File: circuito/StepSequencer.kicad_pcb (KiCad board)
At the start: 2 copper layers, 126.5 x 117.1 mm, 89 parts, among them P1 BEAGLEBONE_BLACK, P2 CONN_01X01, P3 CONN_01X01, P4 CONN_01X01, P5 CONN_01X01, SW0 SW_PUSH, SW1 SW_PUSH, SW10 SW_PUSH, SW11 SW_PUSH, SW12 SW_PUSH, SW13 SW_PUSH, SW14 SW_PUSH, SW15 SW_PUSH, SW2 SW_PUSH, SW3 SW_PUSH, SW4 SW_PUSH, SW5 SW_PUSH, SW6 SW_PUSH, SW7 SW_PUSH, SW8 SW_PUSH, SW9 SW_PUSH

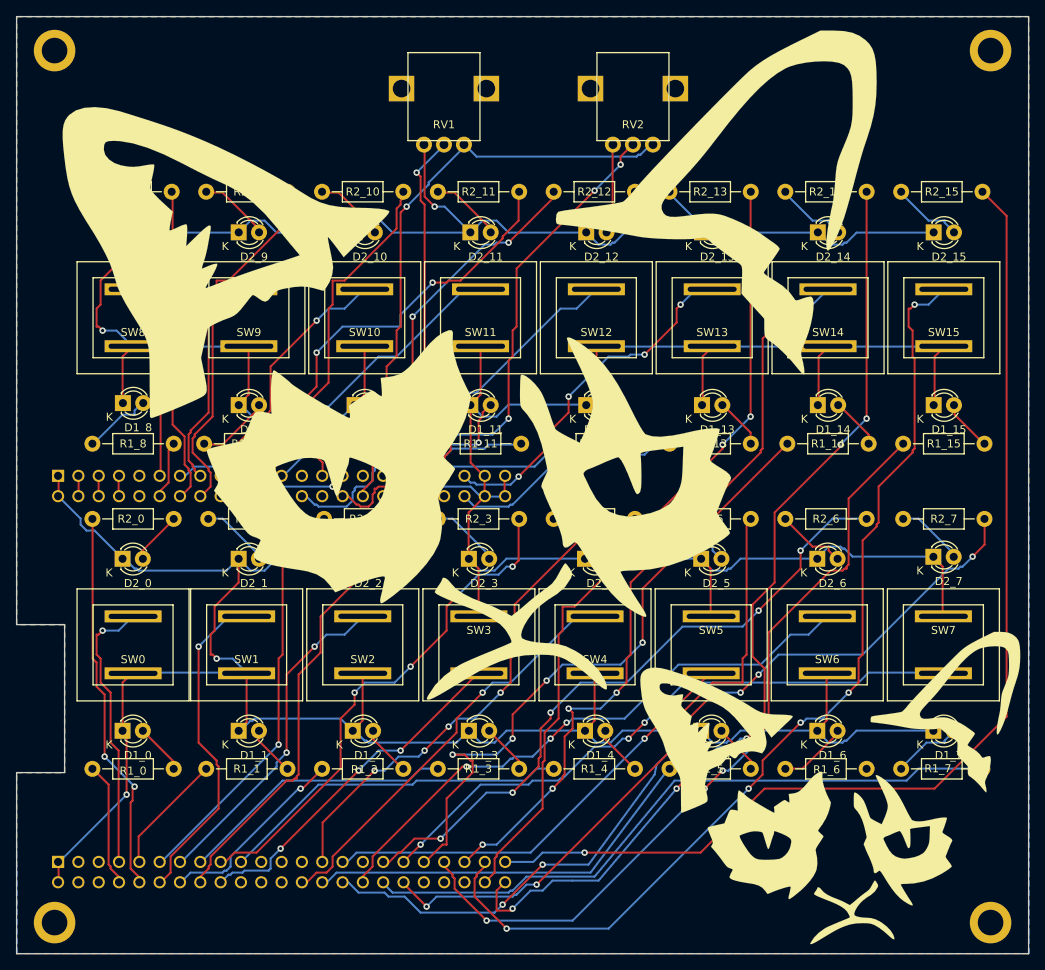
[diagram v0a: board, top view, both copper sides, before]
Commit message: arreglados huecos corte botones y botones footprints
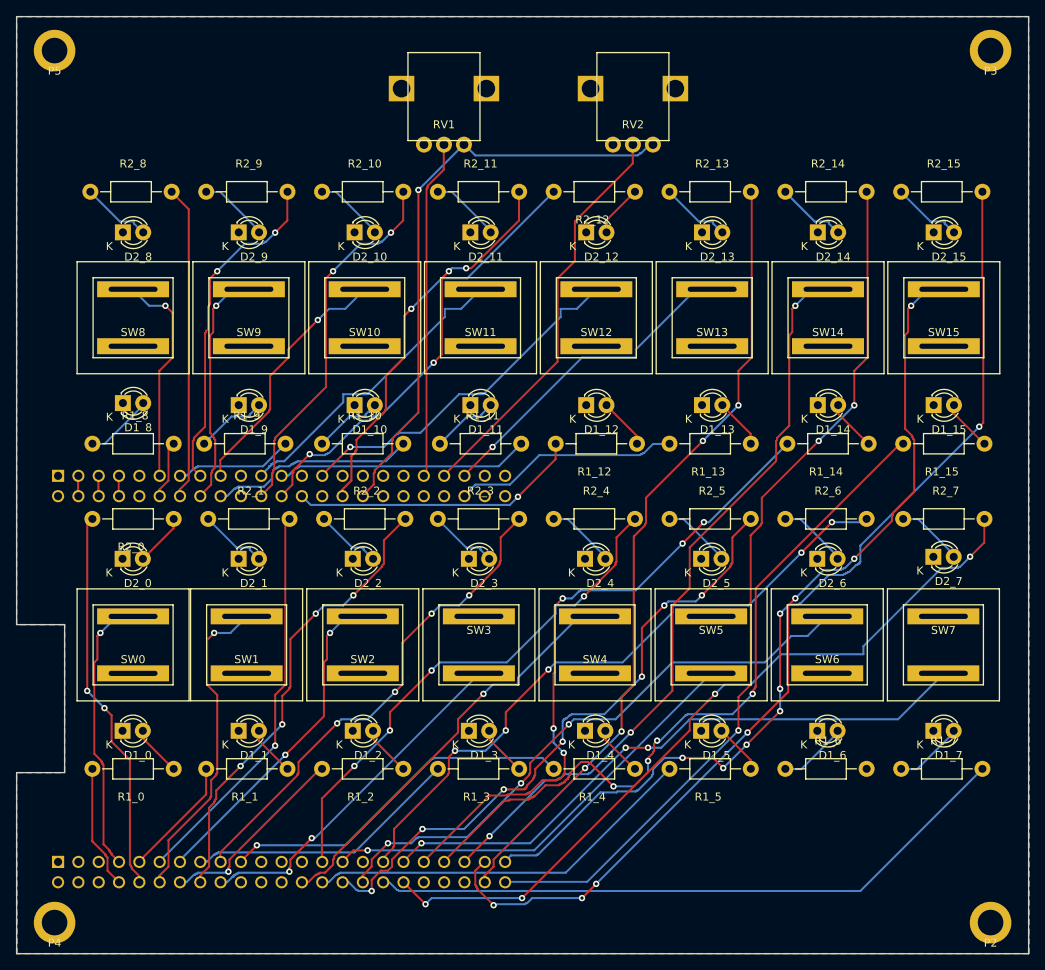
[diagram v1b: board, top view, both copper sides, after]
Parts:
- removed G***: LOGO, StepSequencer:GATO3
- removed G***: LOGO, StepSequencer:GATO2
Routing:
- net GNDD: track 700.0 -> 0.00 mm, vias 4 -> 0
- net /led2_15: track 137.1 -> 121.4 mm, vias 1 -> 7
- net /led2_11: track 63.6 -> 54.3 mm, vias 2 -> 4
- net /led2_14: track 120.5 -> 111.2 mm, vias 6 -> 3
- net /led2_5: track 87.9 -> 80.1 mm, vias 3 -> 7
- net /led1_15: track 98.5 -> 91.2 mm
- net /btn15: track 123.9 -> 116.8 mm, vias 5 -> 7
- net /btn12: track 49.2 -> 44.6 mm, vias 3 -> 1
- net /led2_12: track 55.3 -> 50.9 mm, vias 2 -> 1
- net /btn13: track 45.0 -> 41.3 mm, vias 4 -> 1
- net /pot1: track 54.3 -> 51.3 mm, vias 4 -> 0
- net /led2_3: track 64.6 -> 61.7 mm
- net Net-(D1_11-Pad2): track 10.4 -> 8.57 mm, vias 1 -> 0
- net /btn9: track 31.7 -> 30.1 mm
- net /btn14: track 95.7 -> 94.4 mm, vias 5 -> 3
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
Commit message: Arreglados huecos de botones, agregando modelos 3d de botones y pots
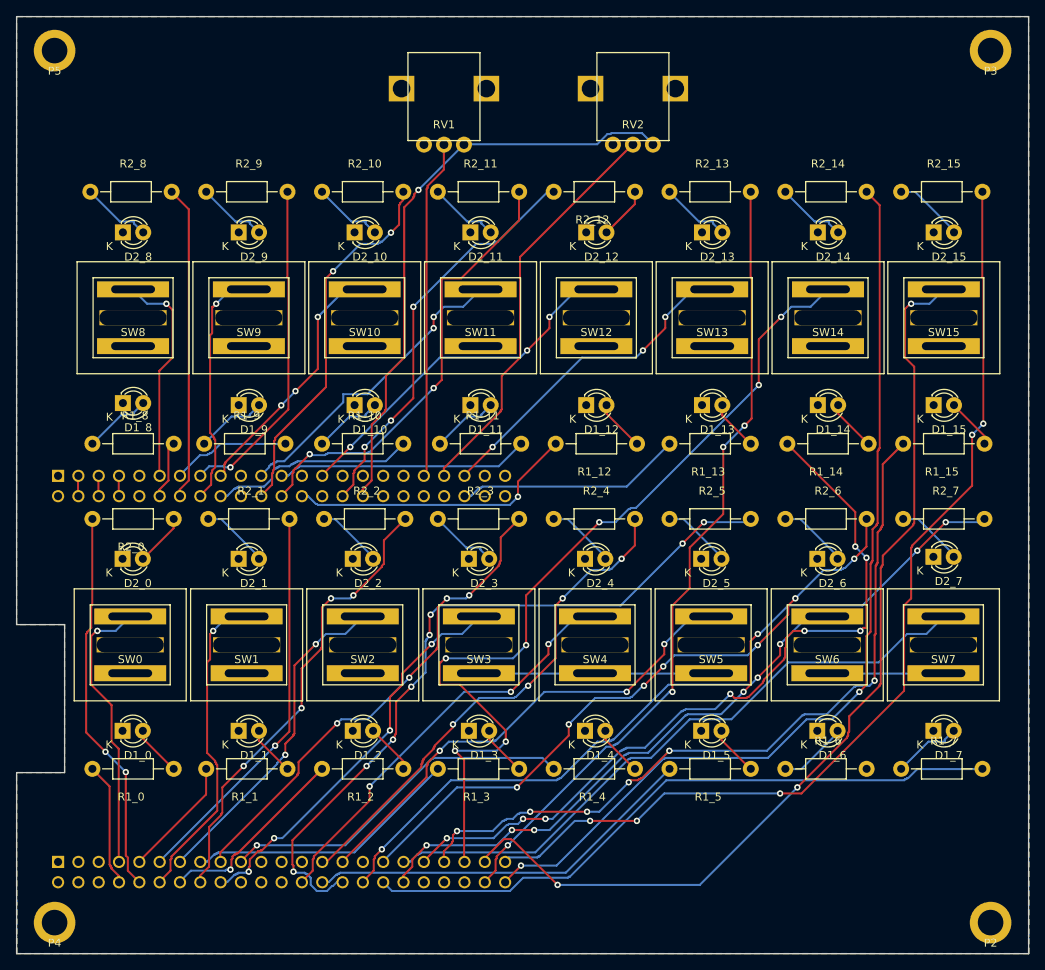
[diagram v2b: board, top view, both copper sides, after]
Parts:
- moved SW0 0.36 mm to (97.5, 115.3)
- turned SW3 to 0 degrees
- turned SW5 to 0 degrees
- turned SW7 to 0 degrees
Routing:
- net GNDD: track 0.00 -> 43.9 mm
- net /btn14: track 94.4 -> 110.9 mm, vias 3 -> 7
- net /led1_14: track 81.4 -> 96.6 mm, vias 5 -> 8
- net /led2_5: track 80.1 -> 92.6 mm, vias 7 -> 8
- net /led2_14: track 111.2 -> 118.5 mm, vias 3 -> 2
- net /btn3: track 44.2 -> 50.3 mm, vias 2 -> 4
- net /btn5: track 55.9 -> 60.6 mm, vias 1 -> 3
- net /led1_15: track 91.2 -> 95.6 mm, vias 4 -> 6
- net /led2_15: track 121.4 -> 125.4 mm, vias 7 -> 5
- net /btn15: track 116.8 -> 120.2 mm, vias 7 -> 3
- net /btn7: track 77.4 -> 80.4 mm, vias 3 -> 0
- net /led2_4: track 65.4 -> 63.6 mm
- net /led2_11: track 54.3 -> 56.1 mm, vias 4 -> 2
- net /led2_7: track 97.0 -> 95.7 mm, vias 4 -> 7
- net /led2_6: track 83.0 -> 81.8 mm, vias 5 -> 7
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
